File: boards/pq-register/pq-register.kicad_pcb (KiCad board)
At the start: 2 copper layers, 114.3 x 134.2 mm, 688 parts, among them P1 Card Edge, Q1 MMBT5401, Q10 MMBT5401, Q100 MMBT5401, Q101 MMBT5401, Q102 MMBT5401, Q103 MMBT5401, Q11 MMBT5401, Q12 MMBT5401, Q13 MMBT5401, Q14 MMBT5401, Q15 MMBT5401, Q16 MMBT5401, Q17 MMBT5401, Q18 MMBT5401, Q19 MMBT5401, Q2 MMBT5401, Q20 MMBT5401, Q21 MMBT5401, Q22 MMBT5401, Q23 MMBT5401, Q24 MMBT5401, Q25 MMBT5401, Q26 MMBT5401, Q27 MMBT5401, Q28 MMBT5401, Q29 MMBT5401, Q3 MMBT5401, Q30 MMBT5401, Q31 MMBT5401, Q32 MMBT5401, Q33 MMBT5401, Q34 MMBT5401, Q35 MMBT5401, Q36 MMBT5401, Q37 MMBT5401, Q38 MMBT5401, Q39 MMBT5401, Q4 MMBT5401, Q40 MMBT5401, Q41 MMBT5401, Q42 MMBT5401, Q43 MMBT5401, Q44 MMBT5401, Q45 MMBT5401, Q46 MMBT5401, Q47 MMBT5401, Q48 MMBT5401, Q49 MMBT5401, Q5 MMBT5401, Q50 MMBT5401, Q51 MMBT5401, Q52 MMBT5401, Q53 MMBT5401, Q54 MMBT5401, Q55 MMBT5401, Q56 MMBT5401, Q57 MMBT5401, Q58 MMBT5401, Q59 MMBT5401, Q6 MMBT5401, Q60 MMBT5401, Q61 MMBT5401, Q62 MMBT5401, Q63 MMBT5401, Q64 MMBT5401, Q65 MMBT5401, Q66 MMBT5401, Q67 MMBT5401, Q68 MMBT5401, Q69 MMBT5401, Q7 MMBT5401, Q70 MMBT5401, Q71 MMBT5401, Q72 MMBT5401, Q73 MMBT5401, Q74 MMBT5401, Q75 MMBT5401, Q76 MMBT5401, Q77 MMBT5401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

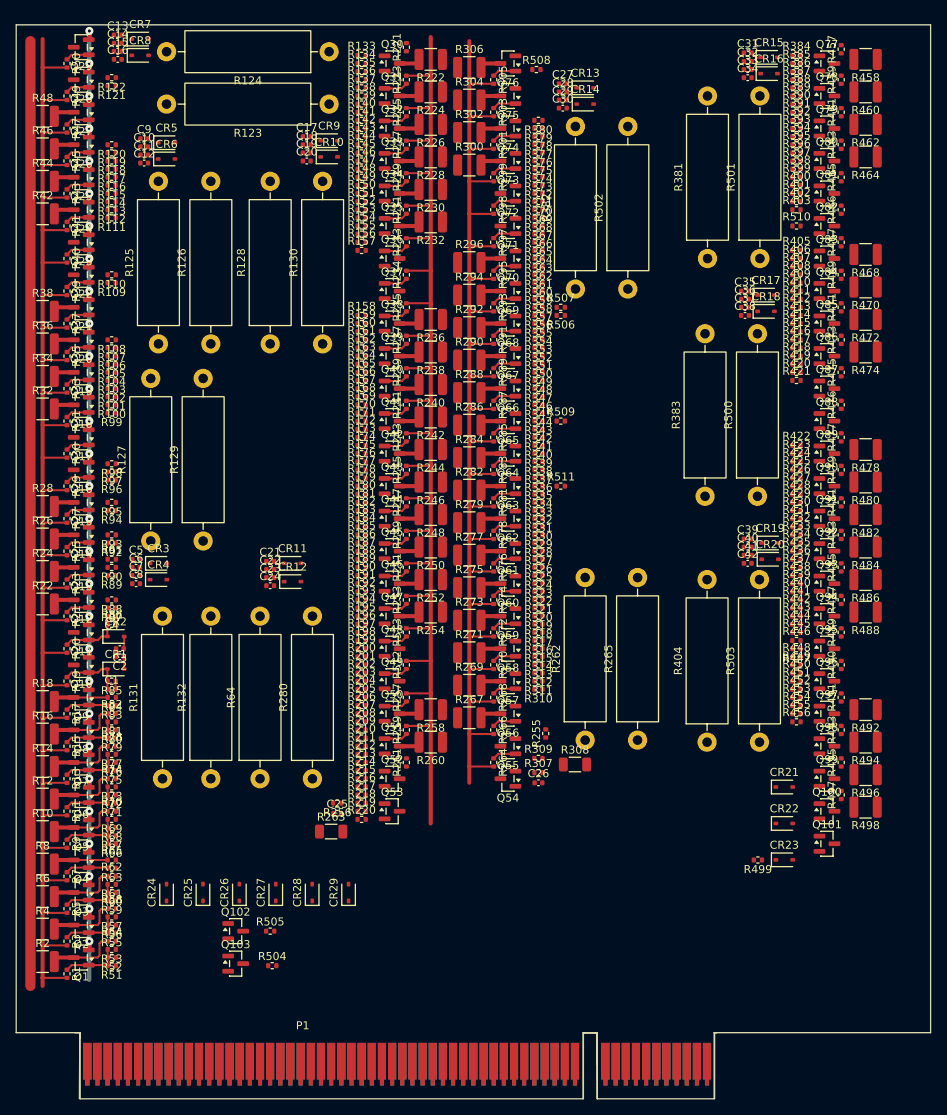
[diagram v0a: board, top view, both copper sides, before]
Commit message: Densify layout and define board outline.
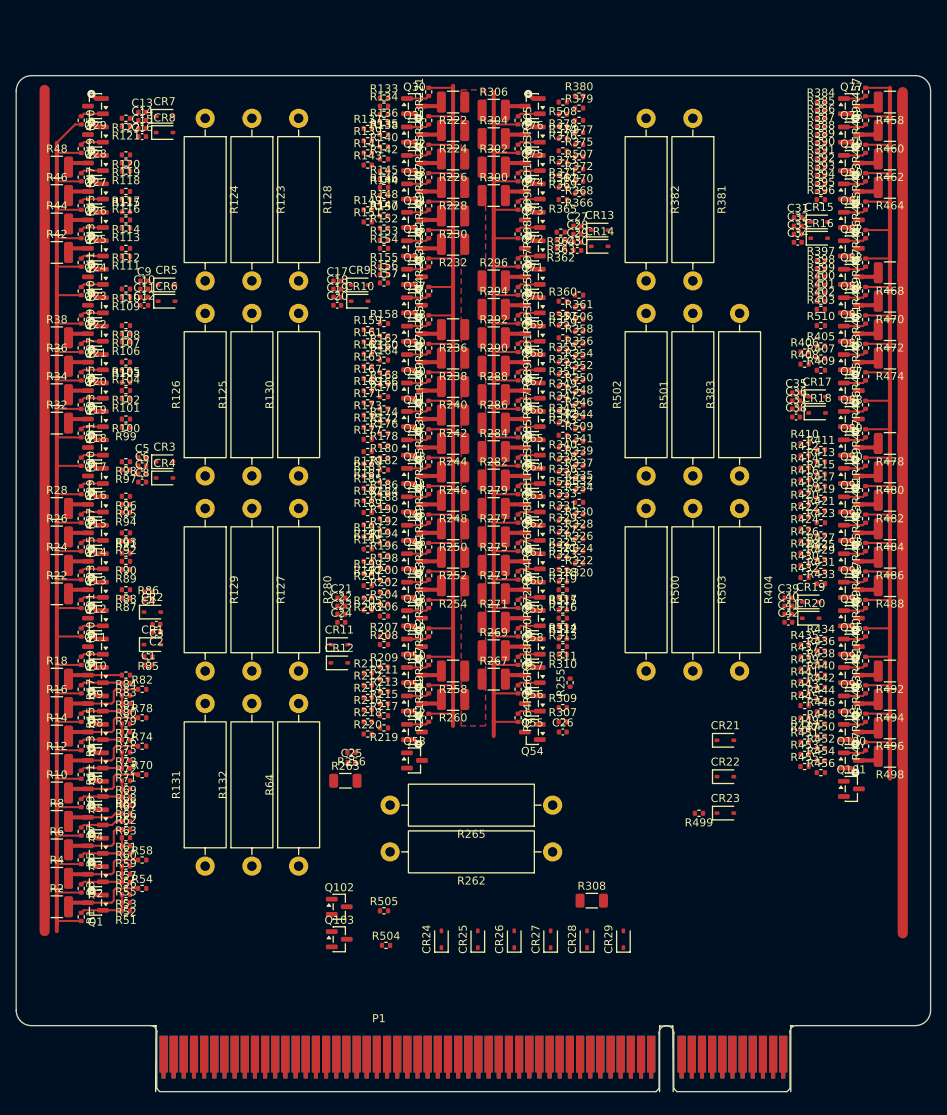
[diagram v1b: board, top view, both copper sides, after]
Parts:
- moved CR24 34.8 mm to (129.4, 158.8)
- moved CR27 34.8 mm to (143.0, 158.8)
- moved CR29 34.8 mm to (152.1, 158.8)
- moved CR26 34.8 mm to (138.5, 158.8)
- moved CR28 34.8 mm to (147.6, 158.8)
- moved CR25 34.8 mm to (133.9, 158.8)
- moved R280 33.8 mm to (111.5, 104.9), turned to -90 degrees
- moved R503 30.4 mm to (160.8, 104.9), turned to -90 degrees
- moved R404 29.5 mm to (166.6, 104.9), turned to -90 degrees
- moved R501 28.4 mm to (160.8, 100.8)
- moved R128 28.4 mm to (111.5, 56.1), turned to -90 degrees
- moved R502 23.5 mm to (154.9, 100.8)
- moved R382 23.1 mm to (154.9, 56.1), turned to -90 degrees
- moved C31 21.5 mm to (173.9, 68.5)
- moved C32 21.5 mm to (173.9, 69.6)
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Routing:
- net +15V: track 528.9 -> 645.2 mm
- net -20V: track 118.1 -> 210.3 mm
- net GND: track 148.1 -> 163.3 mm, vias 29 -> 98
- net Net-(CR2-K): track 8.03 -> 2.85 mm
- net Net-(CR1-K): track 8.03 -> 2.85 mm
- net Net-(Q98-B): track 0.00 -> 2.85 mm
- net Net-(Q90-B): track 0.00 -> 2.85 mm
- net Net-(Q84-B): track 0.00 -> 2.85 mm
- net Net-(Q100-B): track 0.00 -> 2.85 mm
- net Net-(CR19-K): track 0.00 -> 2.85 mm
- net Net-(Q97-B): track 0.00 -> 2.85 mm
- net Net-(Q94-B): track 0.00 -> 2.85 mm
- net Net-(Q93-B): track 0.00 -> 2.85 mm
- net Net-(Q92-B): track 0.00 -> 2.85 mm
- net Net-(Q91-B): track 0.00 -> 2.85 mm
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- added copper zone on F.Cu, net -20V
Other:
- board size 114.3 x 134.2 mm -> 114.3 x 127 mm
